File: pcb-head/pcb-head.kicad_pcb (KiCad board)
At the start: 2 copper layers, 24.5 x 4.5 mm, 4 parts, among them J1 Conn_01x01, J2 Conn_01x01

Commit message: Wire head pcb.
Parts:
- turned D1 to 0 degrees
- turned D2 to 180 degrees
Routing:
- net Net-(D1-Pad2): track 0.00 -> 21.6 mm
- net /-: track 0.00 -> 8.70 mm
- net /+: track 0.00 -> 6.47 mm
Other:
- board text added: "+"
- board text added: "-"

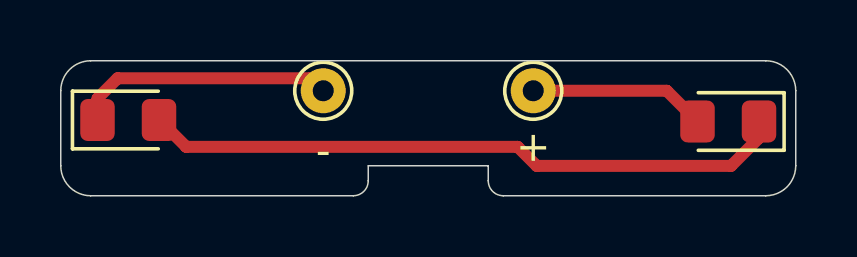
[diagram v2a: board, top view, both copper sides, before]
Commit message: Migrate to KiCad 6.
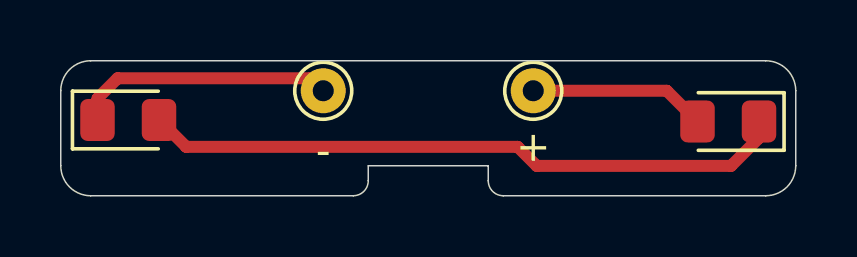
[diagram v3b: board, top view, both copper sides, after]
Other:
- net class Default removed

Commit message: Add proper mousebites position.
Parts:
- added REF**: Tab, kikit:Tab, F.Cu at (175.0, 102.2)
- added REF**: Tab, kikit:Tab, F.Cu at (154.5, 99.8)
- added REF**: Tab, kikit:Tab, F.Cu at (170.2, 104.8)
- added REF**: Tab, kikit:Tab, F.Cu at (170.2, 99.8)
- added REF**: Tab, kikit:Tab, F.Cu at (154.5, 104.8)
- added REF**: Tab, kikit:Tab, F.Cu at (150.0, 102.2)
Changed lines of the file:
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@@
 (kicad_pcb (version 20211014) (generator pcbnew)
   (general
-    (thickness 0.8)
+    (thickness 0.6)
   )
   (paper "A4")
@@
   )
   (setup
+    (stackup
+      (layer "F.SilkS" (type "Top Silk Screen"))
+      (layer "F.Paste" (type "Top Solder Paste"))
+      (layer "F.Mask" (type "Top Solder Mask") (thickness 0.01))
+      (layer "F.Cu" (type "copper") (thickness 0.035))
+      (layer "dielectric 1" (type "core") (thickness 0.51) (material "FR4") (epsilon_r 4.5) (loss_tangent 0.02))
+      (layer "B.Cu" (type "copper") (thickness 0.035))
+      (layer "B.Mask" (type "Bottom Solder Mask") (thickness 0.01))
+      (layer "B.Paste" (type "Bottom Solder Paste"))
+      (layer "B.SilkS" (type "Bottom Silk Screen"))
+      (copper_finish "None")
+      (dielectric_constraints no)
+    )
     (pad_to_mask_clearance 0)
     (pcbplotparams
@@
     (fp_line (start -1.86 -0.96) (end -1.86 0.96) (layer "F.SilkS") (width 0.12))
     (fp_line (start -1.86 0.96) (end 1 0.96) (layer "F.SilkS") (width 0.12))
+    (fp_line (start -1.85 -0.95) (end 1.85 -0.95) (layer "F.CrtYd") (width 0.05))
     (fp_line (start 1.85 0.95) (end -1.85 0.95) (layer "F.CrtYd") (width 0.05))
     (fp_line (start 1.85 -0.95) (end 1.85 0.95) (layer "F.CrtYd") (width 0.05))
-    (fp_line (start -1.85 -0.95) (end 1.85 -0.95) (layer "F.CrtYd") (width 0.05))
     (fp_line (start -1.85 0.95) (end -1.85 -0.95) (layer "F.CrtYd") (width 0.05))
-    (fp_line (start -1 0.6) (end 1 0.6) (layer "F.Fab") (width 0.1))
     (fp_line (start -1 -0.3) (end -1 0.6) (layer "F.Fab") (width 0.1))
+    (fp_line (start 1 0.6) (end 1 -0.6) (layer "F.Fab") (width 0.1))
     (fp_line (start -0.7 -0.6) (end -1 -0.3) (layer "F.Fab") (width 0.1))
     (fp_line (start 1 -0.6) (end -0.7 -0.6) (layer "F.Fab") (width 0.1))
-    (fp_line (start 1 0.6) (end 1 -0.6) (layer "F.Fab") (width 0.1))
+    (fp_line (start -1 0.6) (end 1 0.6) (layer "F.Fab") (width 0.1))
     (pad "1" smd roundrect locked (at -1.025 0) (size 1.15 1.4) (layers "F.Cu" "F.Paste" "F.Mask") (roundrect_rratio 0.217391)
       (net 2 "/-") (pinfunction "K") (pintype "passive"))
     (pad "2" smd roundrect locked (at 1.025 0) (size 1.15 1.4) (layers "F.Cu" "F.Paste" "F.Mask") (roundrect_rratio 0.217391)
       (net 1 "Net-(D1-Pad2)") (pinfunction "A") (pintype "passive"))
-    (model "${KISYS3DMOD}/LED_SMD.3dshapes/LED_0805_2012Metric.wrl"
+    (model "${KICAD6_3DMODEL_DIR}/LED_SMD.3dshapes/LED_0805_2012Metric.wrl"
       (offset (xyz 0 0 0))
       (scale (xyz 1 1 1))
@@
       (effects (font (size 0.5 0.5) (thickness 0.08)))
     )
-    (fp_line (start -1.86 0.96) (end 1 0.96) (layer "F.SilkS") (width 0.12))
     (fp_line (start -1.86 -0.96) (end -1.86 0.96) (layer "F.SilkS") (width 0.12))
     (fp_line (start 1 -0.96) (end -1.86 -0.96) (layer "F.SilkS") (width 0.12))
+    (fp_line (start -1.86 0.96) (end 1 0.96) (layer "F.SilkS") (width 0.12))
+    (fp_line (start 1.85 0.95) (end -1.85 0.95) (layer "F.CrtYd") (width 0.05))
     (fp_line (start -1.85 0.95) (end -1.85 -0.95) (layer "F.CrtYd") (width 0.05))
-    (fp_line (start 1.85 0.95) (end -1.85 0.95) (layer "F.CrtYd") (width 0.05))
     (fp_line (start 1.85 -0.95) (end 1.85 0.95) (layer "F.CrtYd") (width 0.05))
     (fp_line (start -1.85 -0.95) (end 1.85 -0.95) (layer "F.CrtYd") (width 0.05))
+    (fp_line (start -0.7 -0.6) (end -1 -0.3) (layer "F.Fab") (width 0.1))
+    (fp_line (start -1 -0.3) (end -1 0.6) (layer "F.Fab") (width 0.1))
     (fp_line (start 1 -0.6) (end -0.7 -0.6) (layer "F.Fab") (width 0.1))
-    (fp_line (start -1 -0.3) (end -1 0.6) (layer "F.Fab") (width 0.1))
     (fp_line (start 1 0.6) (end 1 -0.6) (layer "F.Fab") (width 0.1))
     (fp_line (start -1 0.6) (end 1 0.6) (layer "F.Fab") (width 0.1))
-    (fp_line (start -0.7 -0.6) (end -1 -0.3) (layer "F.Fab") (width 0.1))
     (pad "1" smd roundrect locked (at -1.025 0 180) (size 1.15 1.4) (layers "F.Cu" "F.Paste" "F.Mask") (roundrect_rratio 0.217391)
       (net 1 "Net-(D1-Pad2)") (pinfunction "K") (pintype "passive"))
     (pad "2" smd roundrect locked (at 1.025 0 180) (size 1.15 1.4) (layers "F.Cu" "F.Paste" "F.Mask") (roundrect_rratio 0.217391)
       (net 3 "/+") (pinfunction "A") (pintype "passive"))
-    (model "${KISYS3DMOD}/LED_SMD.3dshapes/LED_0805_2012Metric.wrl"
+    (model "${KICAD6_3DMODEL_DIR}/LED_SMD.3dshapes/LED_0805_2012Metric.wrl"
       (offset (xyz 0 0 0))
       (scale (xyz 1 1 1))
@@
     )
   )
+  (footprint "kikit:Tab" (layer "F.Cu")
+    (at 175 102.25 180)
+    (descr "A symbol representing annotation for tab placement")
+    (attr exclude_from_pos_files exclude_from_bom)
+    (fp_text reference "REF**" (at 0 -2) (layer "F.SilkS") hide
+      (effects (font (size 1 1) (thickness 0.15)))
+    )
+    (fp_text value "Tab" (at -2.75 -1) (layer "Dwgs.User")
+      (effects (font (size 1.2 1.2) (thickness 0.2)))
+    )
+    (fp_text user "KIKIT: width: 2mm" (at -5.5 0 90) (layer "Dwgs.User")
+      (effects (font (size 1 1) (thickness 0.15)))
+    )
+    (fp_line (start 0.25 0) (end -0.75 1) (layer "Dwgs.User") (width 0.3))
+    (fp_line (start 0.25 0) (end -0.75 -1) (layer "Dwgs.User") (width 0.3))
+    (fp_line (start 0.25 1) (end 0.25 -1) (layer "Dwgs.User") (width 0.3))
+    (fp_line (start 0.25 0) (end -2.75 0) (layer "Dwgs.User") (width 0.3))
+  )
+  (footprint "kikit:Tab" (layer "F.Cu")
+    (at 154.5 99.75 -90)
+    (descr "A symbol representing annotation for tab placement")
+    (attr exclude_from_pos_files exclude_from_bom)
+    (fp_text reference "REF**" (at 0 -2 90) (layer "F.SilkS") hide
+      (effects (font (size 1 1) (thickness 0.15)))
+    )
+    (fp_text value "Tab" (at -2.75 -1 90) (layer "Dwgs.User")
+      (effects (font (size 1.2 1.2) (thickness 0.2)))
+    )
+    (fp_text user "KIKIT: width: 3mm" (at -5.5 0) (layer "Dwgs.User")
+      (effects (font (size 1 1) (thickness 0.15)))
+    )
+    (fp_line (start 0.25 1) (end 0.25 -1) (layer "Dwgs.User") (width 0.3))
+    (fp_line (start 0.25 0) (end -0.75 1) (layer "Dwgs.User") (width 0.3))
+    (fp_line (start 0.25 0) (end -0.75 -1) (layer "Dwgs.User") (width 0.3))
+    (fp_line (start 0.25 0) (end -2.75 0) (layer "Dwgs.User") (width 0.3))
+  )
+  (footprint "kikit:Tab" (layer "F.Cu")
+    (at 170.25 104.75 90)
+    (descr "A symbol representing annotation for tab placement")
+    (attr exclude_from_pos_files exclude_from_bom)
+    (fp_text reference "REF**" (at 0 -2 90) (layer "F.SilkS") hide
+      (effects (font (size 1 1) (thickness 0.15)))
+    )
+    (fp_text value "Tab" (at -2.75 -1 90) (layer "Dwgs.User")
+      (effects (font (size 1.2 1.2) (thickness 0.2)))
+    )
+    (fp_text user "KIKIT: width: 3mm" (at -5.5 0) (layer "Dwgs.User")
+      (effects (font (size 1 1) (thickness 0.15)))
+    )
+    (fp_line (start 0.25 0) (end -0.75 1) (layer "Dwgs.User") (width 0.3))
+    (fp_line (start 0.25 1) (end 0.25 -1) (layer "Dwgs.User") (width 0.3))
+    (fp_line (start 0.25 0) (end -2.75 0) (layer "Dwgs.User") (width 0.3))
+    (fp_line (start 0.25 0) (end -0.75 -1) (layer "Dwgs.User") (width 0.3))
+  )
+  (footprint "kikit:Tab" (layer "F.Cu")
+    (at 170.25 99.75 -90)
+    (descr "A symbol representing annotation for tab placement")
+    (attr exclude_from_pos_files exclude_from_bom)
+    (fp_text reference "REF**" (at 0 -2 90) (layer "F.SilkS") hide
+      (effects (font (size 1 1) (thickness 0.15)))
+    )
+    (fp_text value "Tab" (at -2.75 -1 90) (layer "Dwgs.User")
+      (effects (font (size 1.2 1.2) (thickness 0.2)))
+    )
+    (fp_text user "KIKIT: width: 3mm" (at -5.5 0) (layer "Dwgs.User")
+      (effects (font (size 1 1) (thickness 0.15)))
+    )
+    (fp_line (start 0.25 0) (end -2.75 0) (layer "Dwgs.User") (width 0.3))
+    (fp_line (start 0.25 0) (end -0.75 1) (layer "Dwgs.User") (width 0.3))
+    (fp_line (start 0.25 0) (end -0.75 -1) (layer "Dwgs.User") (width 0.3))
+    (fp_line (start 0.25 1) (end 0.25 -1) (layer "Dwgs.User") (width 0.3))
+  )
+  (footprint "kikit:Tab" (layer "F.Cu")
+    (at 154.5 104.75 90)
+    (descr "A symbol representing annotation for tab placement")
+    (attr exclude_from_pos_files exclude_from_bom)
+    (fp_text reference "REF**" (at 0 -2 90) (layer "F.SilkS") hide
+      (effects (font (size 1 1) (thickness 0.15)))
+    )
+    (fp_text value "Tab" (at -2.75 -1 90) (layer "Dwgs.User")
+      (effects (font (size 1.2 1.2) (thickness 0.2)))
+    )
+    (fp_text user "KIKIT: width: 3mm" (at -5.5 0) (layer "Dwgs.User")
+      (effects (font (size 1 1) (thickness 0.15)))
+    )
+    (fp_line (start 0.25 0) (end -2.75 0) (layer "Dwgs.User") (width 0.3))
+    (fp_line (start 0.25 0) (end -0.75 -1) (layer "Dwgs.User") (width 0.3))
+    (fp_line (start 0.25 0) (end -0.75 1) (layer "Dwgs.User") (width 0.3))
+    (fp_line (start 0.25 1) (end 0.25 -1) (layer "Dwgs.User") (width 0.3))
+  )
+  (footprint "kikit:Tab" (layer "F.Cu")
+    (at 150 102.25)
+    (descr "A symbol representing annotation for tab placement")
+    (attr exclude_from_pos_files exclude_from_bom)
+    (fp_text reference "REF**" (at 0 -2) (layer "F.SilkS") hide
+      (effects (font (size 1 1) (thickness 0.15)))
+    )
+    (fp_text value "Tab" (at -2.75 -1) (layer "Dwgs.User")
+      (effects (font (size 1.2 1.2) (thickness 0.2)))
+    )
+    (fp_text user "KIKIT: width: 2mm" (at -5.5 0 90) (layer "Dwgs.User")
+      (effects (font (size 1 1) (thickness 0.15)))
+    )
+    (fp_line (start 0.25 1) (end 0.25 -1) (layer "Dwgs.User") (width 0.3))
+    (fp_line (start 0.25 0) (end -0.75 -1) (layer "Dwgs.User") (width 0.3))
+    (fp_line (start 0.25 0) (end -0.75 1) (layer "Dwgs.User") (width 0.3))
+    (fp_line (start 0.25 0) (end -2.75 0) (layer "Dwgs.User") (width 0.3))
+  )
   (gr_line (start 165 104.5) (end 173.75 104.5) (layer "Edge.Cuts") (width 0.05))

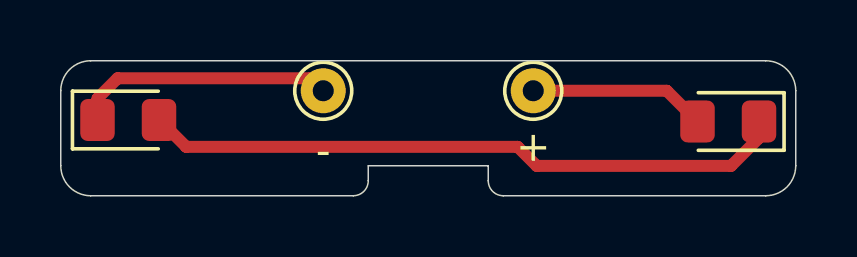
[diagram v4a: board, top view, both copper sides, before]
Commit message: Remove wire stubs.
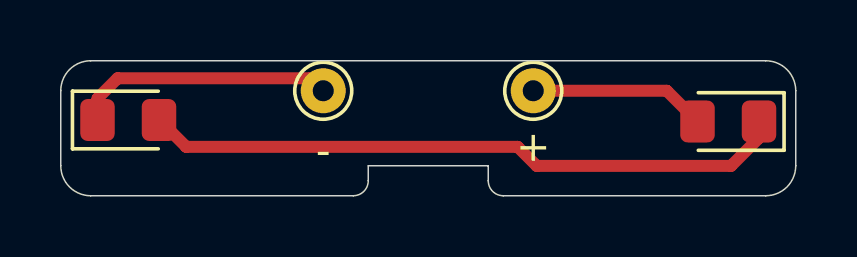
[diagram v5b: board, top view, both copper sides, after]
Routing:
- net /+: track 6.47 -> 5.90 mm
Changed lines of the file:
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@@
   (segment (start 152.146 100.584) (end 158.584 100.584) (width 0.4) (layer "F.Cu") (net 2))
   (segment (start 151.475 101.255) (end 152.146 100.584) (width 0.4) (layer "F.Cu") (net 2))
-  (segment (start 170.45 101) (end 171.475 102.025) (width 0.4) (layer "F.Cu") (net 3))
-  (segment (start 166 100.954) (end 166 101) (width 0.4) (layer "F.Cu") (net 3))
-  (segment (start 166.37 100.584) (end 166 100.954) (width 0.4) (layer "F.Cu") (net 3))
-  (segment (start 166 101) (end 170.45 101) (width 0.4) (layer "F.Cu") (net 3))
+  (segment (start 170.45 101) (end 166 101) (width 0.4) (layer "F.Cu") (net 3))
+  (segment (start 171.475 102.025) (end 170.45 101) (width 0.4) (layer "F.Cu") (net 3))
 )
